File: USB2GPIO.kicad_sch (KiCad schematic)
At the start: 12 parts, among them J1 Conn_01x04, J7 Conn_01x03, J8 Conn_01x03, J9 Conn_01x02

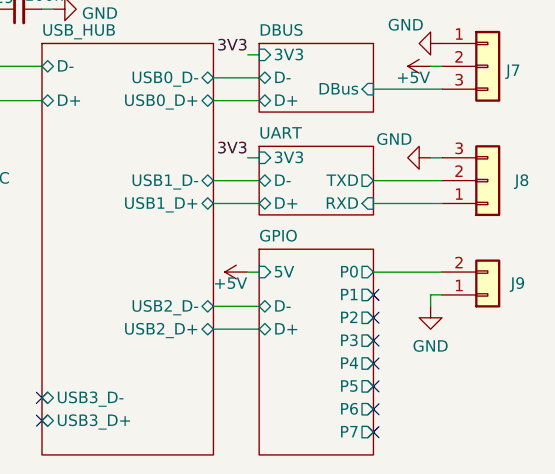
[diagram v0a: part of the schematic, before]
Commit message: Change gpio-pin from P0 to P1
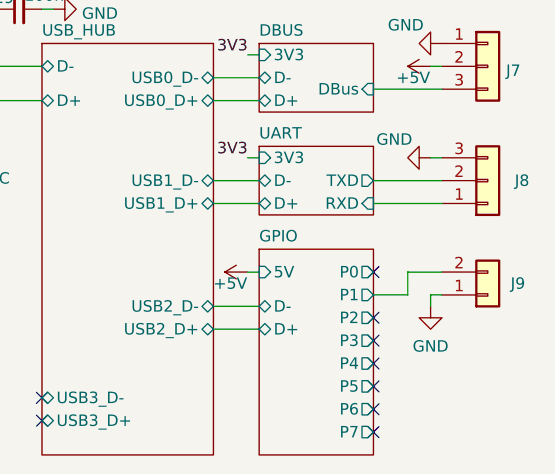
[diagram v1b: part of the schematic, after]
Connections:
- net GPIO/P0: no longer J9.2 (Pin_2)
- net GPIO/P1: now also J9.2 (Pin_2)
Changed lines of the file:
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@@
   )
   (no_connect (at 162.56 120.65))
-  (no_connect (at 162.56 118.11))
+  (no_connect (at 162.56 115.57))
   (no_connect (at 162.56 130.81))
   (no_connect (at 162.56 128.27))
@@
   )
   (wire (pts (xy 119.38 73.66) (xy 119.38 81.28))
+    (stroke (width 0) (type default) (color 0 0 0 0))
+  )
+  (wire (pts (xy 162.56 118.11) (xy 166.37 118.11))
     (stroke (width 0) (type default) (color 0 0 0 0))
   )
@@
     (stroke (width 0) (type default) (color 0 0 0 0))
   )
-  (wire (pts (xy 162.56 115.57) (xy 170.18 115.57))
-    (stroke (width 0) (type default) (color 0 0 0 0))
-  )
   (wire (pts (xy 99.06 87.63) (xy 119.38 87.63))
     (stroke (width 0) (type default) (color 0 0 0 0))
@@
     (stroke (width 0) (type default) (color 0 0 0 0))
   )
+  (wire (pts (xy 166.37 118.11) (xy 166.37 115.57))
+    (stroke (width 0) (type default) (color 0 0 0 0))
+  )
   (wire (pts (xy 168.91 102.87) (xy 170.18 102.87))
     (stroke (width 0) (type default) (color 0 0 0 0))
   )
+  (wire (pts (xy 166.37 115.57) (xy 170.18 115.57))
+    (stroke (width 0) (type default) (color 0 0 0 0))
+  )

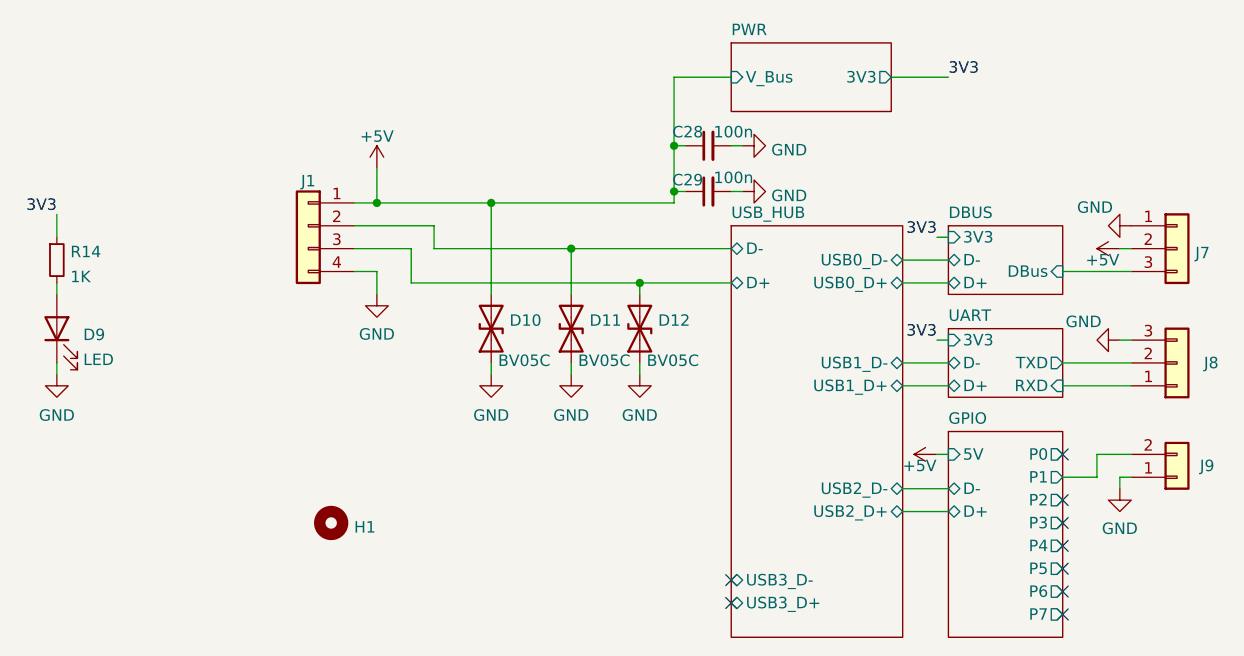
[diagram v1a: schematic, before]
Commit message: Change the map and rebuild the PCB
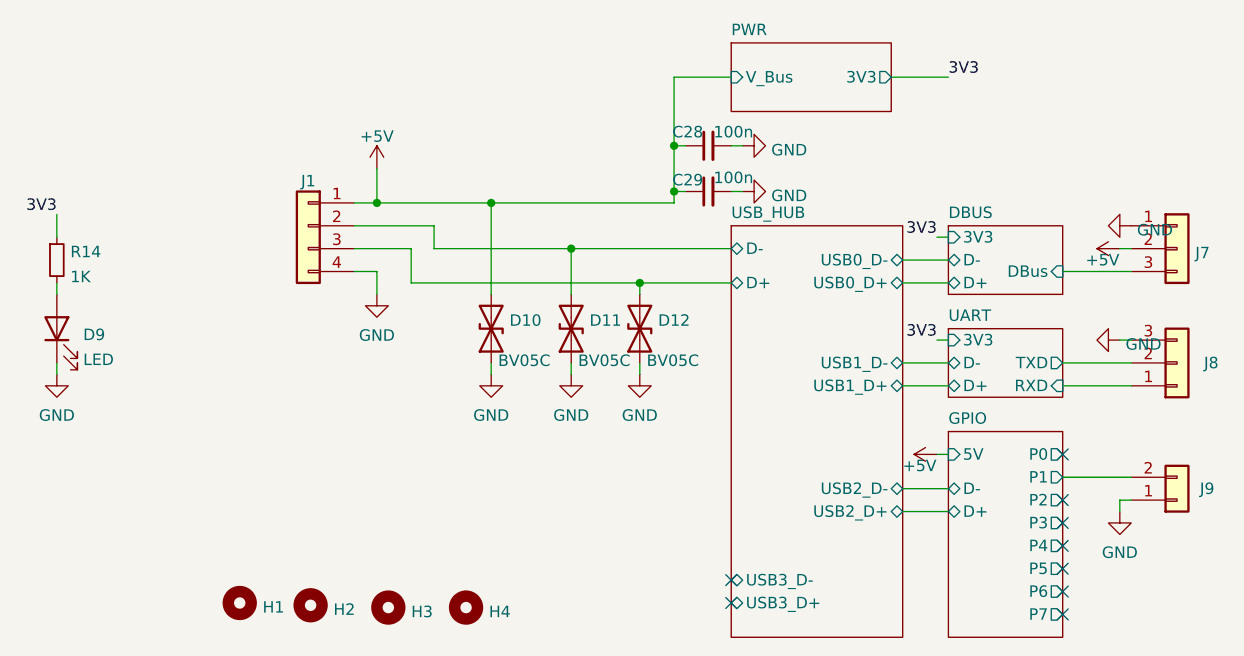
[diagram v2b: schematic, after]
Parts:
- added H2, H3, H4: MountingHole, MountingHole:MountingHole_2.7mm_M2.5, symbol Mechanical:MountingHole
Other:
- moved on the sheet: J9
